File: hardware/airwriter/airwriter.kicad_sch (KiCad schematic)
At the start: 56 parts, among them J1 USB-C 5V in, J2 Mini-DIN-8 to printer, J3 Bring-up USB/UART, J4 Mini-DIN-8 LocalTalk, J6 I2C / Qwiic, SW1 CONFIG/BOOT, SW2 MODE/TEST, U1 ESP32-S3-WROOM-1-N8R2, U2 MAX3490ESA+, U3 MAX3232ESE+, U4 AP7361C-33E, U5 USBLC6-2SC6, U6 SP3485EN-L, U7 PIC12F1840-I/P, U8 SP3485EN-L

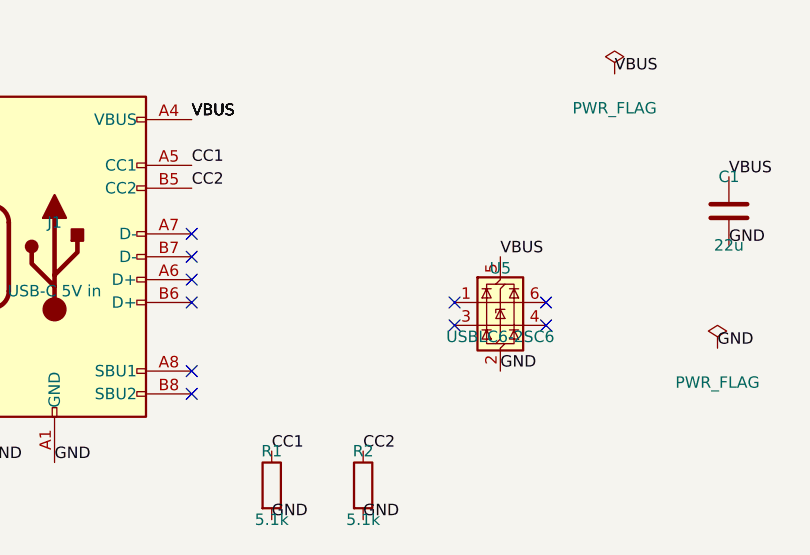
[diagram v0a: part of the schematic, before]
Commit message: Make the USB-C an actual USB port
Spec 2.5 read "USB-C is power only. Flashing and console go over the S3's native USB
peripheral on GPIO19/20 -- expose those on a 4-pin 1.27mm header for bring-up." The
result was a USB connector on the front panel with its data pins tied off, a debug
header nobody can reach without a custom cable, and a two-line USB ESD part sitting
there with four of its six pins no-connected.

D+ and D- now run from J1 through U5 to the S3's native USB peripheral. Both flip
orientations are tied -- A6+B6 and A7+B7 -- which is what a USB 2.0-only device does.
U5's I/O1 is pins 1 and 6 and its I/O2 is pins 3 and 4; each pair is one node inside
the package, so both pins carry the same net and the layout routes through the part.

U5 also moved to sit 2-4mm from J1's data pins instead of 16.7mm, swapping places
with the CC pulldowns. Trace inductance ahead of a clamp is what lets a strike
through, so the ESD part belongs closest to the connector; R1 and R2 only carry a DC
level and can sit further back.

J3 stays as a parallel tap on the same two nets, so there is still a bring-up path if
the connector's data side has a problem on the first spin. J1's silkscreen now reads
USB-C rather than 5V IN, which stopped being true.

Only the S3's native USB is on these pins -- full speed, 12 Mbps -- so the ~60mm run
from J1 to U1 needs no length matching and no impedance control.

SPEC 2.5 amended in place. ERC unchanged at four pre-existing warnings, DRC back to
the single known U1 library mismatch, drill floor 0.300mm, fab regenerated.
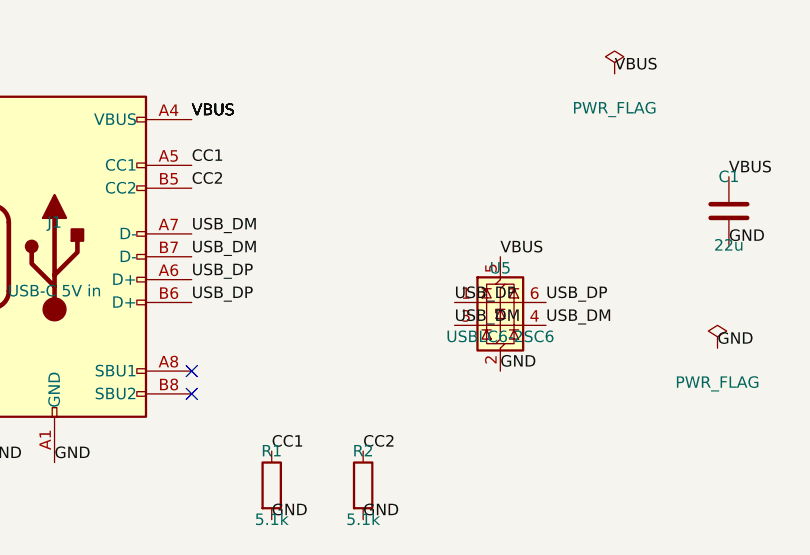
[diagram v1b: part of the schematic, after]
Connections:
- net USB_DM: now also J1.A7 (D-), J1.B7 (D-), U5.3 (I/O2), U5.4 (I/O2)
- net USB_DP: now also J1.A6 (D+), J1.B6 (D+), U5.1 (I/O1), U5.6 (I/O1)
- no-connect marks 39 -> 31
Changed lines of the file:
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@@
   (generator_version "10.0")
   (paper "A3")
-  (no_connect
-    (at 50.8 57.15)
+  (label "USB_DM"
+    (at 50.8 57.15 0)
+    (effects
+      (font
+        (size 1.27 1.27))
+      (justify left bottom))
 )
-  (no_connect
-    (at 50.8 59.69)
+  (label "USB_DM"
+    (at 50.8 59.69 0)
+    (effects
+      (font
+        (size 1.27 1.27))
+      (justify left bottom))
 )
-  (no_connect
-    (at 50.8 62.23)
+  (label "USB_DP"
+    (at 50.8 62.23 0)
+    (effects
+      (font
+        (size 1.27 1.27))
+      (justify left bottom))
 )
-  (no_connect
-    (at 50.8 64.77)
+  (label "USB_DP"
+    (at 50.8 64.77 0)
+    (effects
+      (font
+        (size 1.27 1.27))
+      (justify left bottom))
 )
   (no_connect
@@
     (at 50.8 74.93)
 )
-  (no_connect
-    (at 80.01 64.77)
+  (label "USB_DP"
+    (at 80.01 64.77 0)
+    (effects
+      (font
+        (size 1.27 1.27))
+      (justify left bottom))
+)
+  (label "USB_DM"
+    (at 80.01 67.31 0)
+    (effects
+      (font
+        (size 1.27 1.27))
+      (justify left bottom))
+)
+  (label "USB_DP"
+    (at 90.17 64.77 0)
+    (effects
+      (font
+        (size 1.27 1.27))
+      (justify left bottom))
+)
+  (label "USB_DM"
+    (at 90.17 67.31 0)
+    (effects
+      (font
+        (size 1.27 1.27))
+      (justify left bottom))
 )
   (no_connect
-    (at 80.01 67.31)
-)
-  (no_connect
-    (at 90.17 64.77)
-)
-  (no_connect
-    (at 90.17 67.31)
-)
-  (no_connect

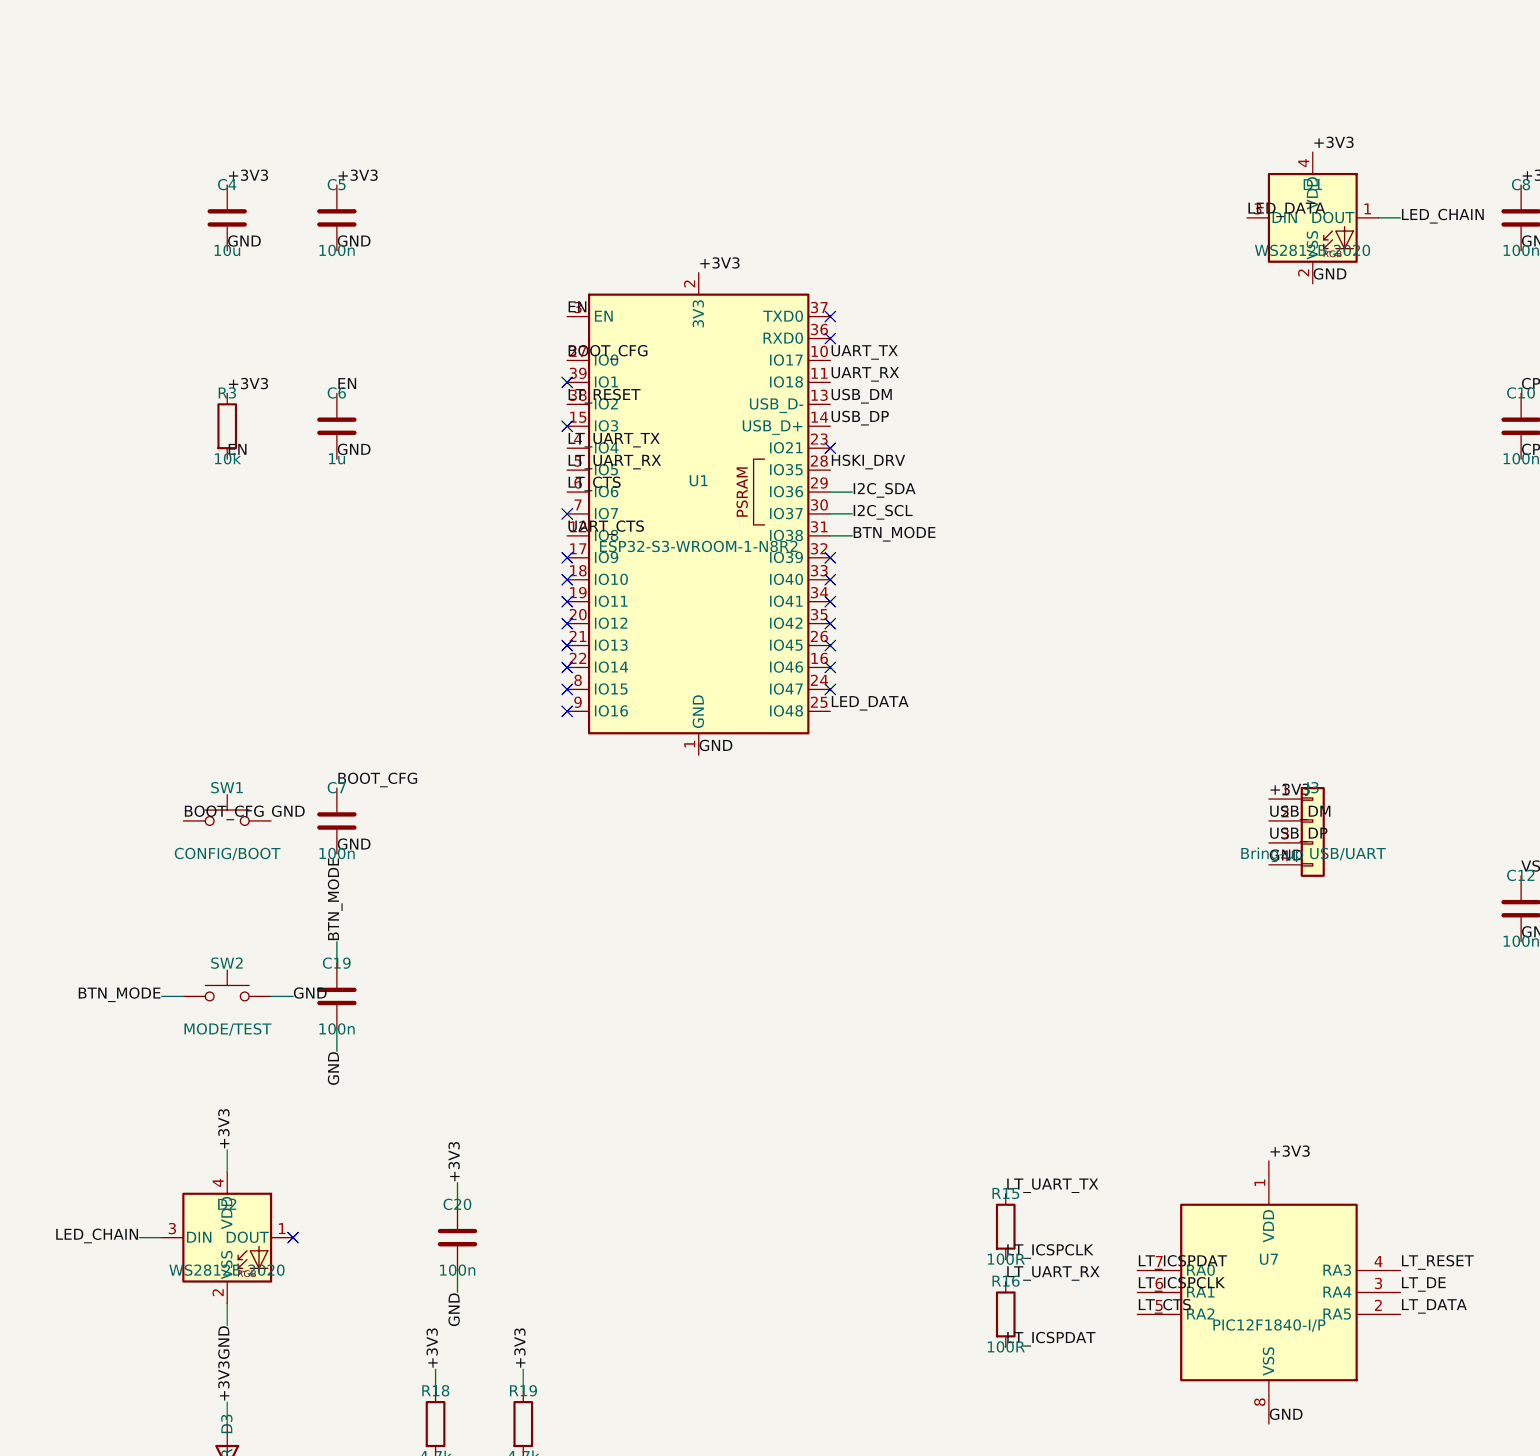
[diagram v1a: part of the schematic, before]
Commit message: Point the indicators at the viewer and make BOOT two pads
Components sit on the face that becomes the underside, so every indicator was firing
away from the person looking at the board. All three are reverse-mount now, emitting
toward the board -- and instead of the hole their footprints expect, they shine into
a bare-FR4 window, which is the logo recipe at small scale.

  D1, D2   WS2812B-2020  ->  SK6812MINI-E   LCSC C5149201, $0.045
  D3       0603 green    ->  LED_1206 ReverseMount
  SW1      B3U-1000P     ->  two bare pads, SolderJumper-2_P1.3mm_Open

The pin numbering changed and the wiring did not. WS2812B-2020 numbers its pins
DOUT-VSS-DIN-VDD; SK6812 numbers them VSS-DIN-VDD-DOUT. But both KiCad symbols put
the same functions at the same coordinates, so swapping lib_id moved every net
correctly and not one label had to move. Checked against the exported netlist.
Firmware is untouched -- SK6812 is the same one-wire protocol at the same 800kbit/s.

BOOT stops being a switch. With the USB-C carrying data, esptool drives the S3 into
download mode over the wire, so the two pads are just insurance you bridge with
tweezers. It also removes the last part that would have wanted a hole in the visible
face. MODE stays a real switch and still faces into the housing; that one is open.

The strip re-spaced -- the SK6812MINI-E is 7.3mm wide against the WS2812B's 3.0 -- and
now runs x 108.9 to 136.3, between mounting hole H3 and the power column.

New trap, documented: D1, D2 and D3 report lib_footprint_mismatch on purpose. Their
library footprints carry a cutout (Edge.Cuts on the SK6812, an NPTH slot on the 1206)
because they are drawn to shine through a hole. Re-importing any of them will punch
the holes back in, same as U1's 0.30mm vias.

DRC is 4 violations and all four are that mismatch. Drill floor 0.300mm, fab
regenerated, ERC unchanged bar the two expected flattened-symbol warnings.
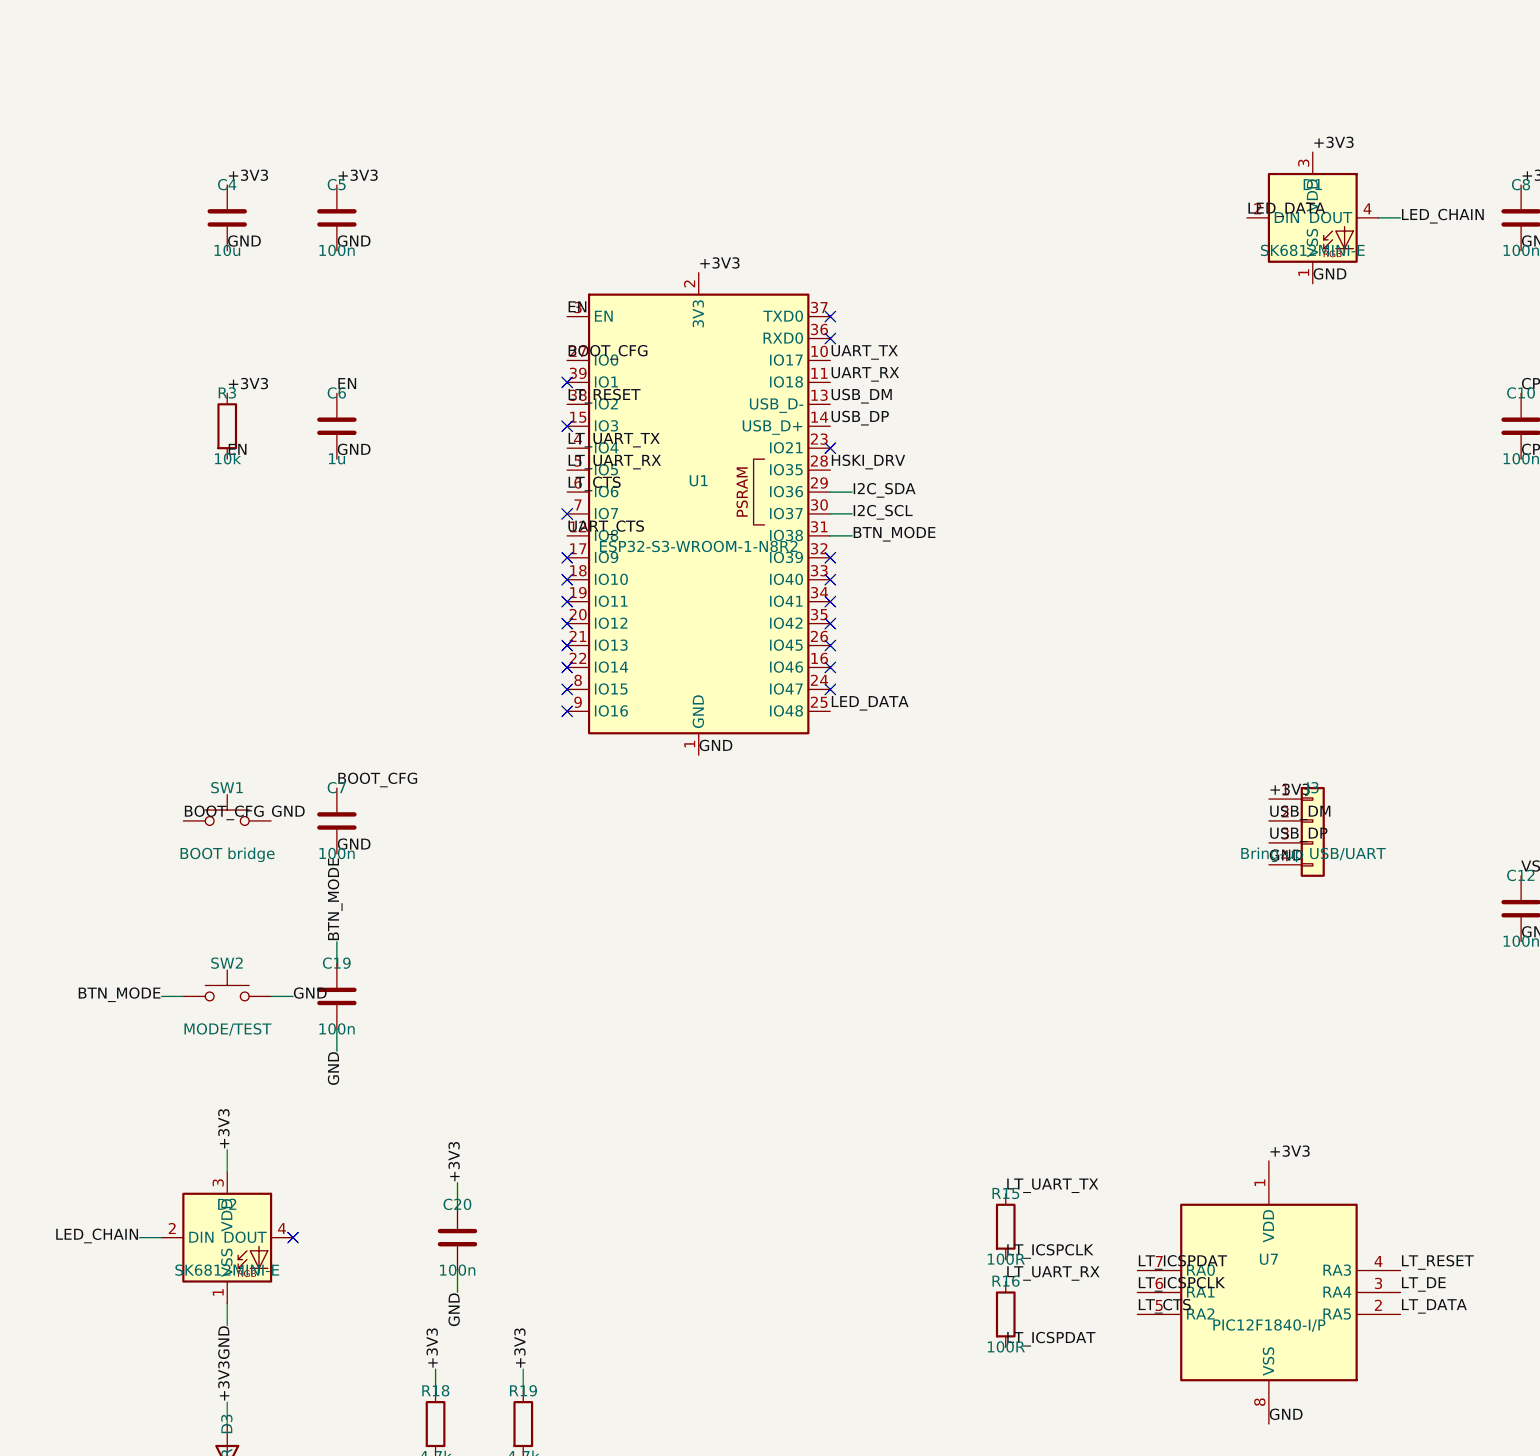
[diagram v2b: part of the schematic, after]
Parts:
- D1, D2: value WS2812B-2020 -> SK6812MINI-E; footprint LED_SMD:LED_WS2812B-2020_PLCC4_2.0x2.0mm -> LED_SMD:LED_SK6812MINI-E_3.2x2.8mm_P1.5mm_ReverseMount; symbol LED:WS2812B-2020 -> LED:SK6812MINI-E; MPN WS2812B-2020 -> SK6812MINI-E; Manufacturer Worldsemi -> OPSCO Optoelectronics
- D3: footprint LED_SMD:LED_0603_1608Metric -> LED_SMD:LED_1206_3216Metric_ReverseMount_Hole1.8x2.4mm
- SW1: value CONFIG/BOOT -> BOOT bridge; footprint Button_Switch_SMD:SW_SPST_B3U-1000P -> Jumper:SolderJumper-2_P1.3mm_Open_Pad1.0x1.5mm; MPN B3U-1000P -> (none); Manufacturer Omron -> none - bare pads on the board
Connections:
- net +3V3: now also D1.3 (VDD), D2.3 (VDD); no longer D1.4 (VDD), D2.4 (VDD)
- net GND: now also D1.1 (VSS), D2.1 (VSS); no longer D1.2 (VSS), D2.2 (VSS)
- net LED_CHAIN: now also D1.4 (DOUT), D2.2 (DIN); no longer D1.1 (DOUT), D2.3 (DIN)
- net LED_DATA: now also D1.2 (DIN); no longer D1.3 (DIN)
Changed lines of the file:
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@@
         (font
           (size 1.27 1.27))))
-    (property "Value" "CONFIG/BOOT"
+    (property "Value" "BOOT bridge"
       (at 149.86 179.07 0)
       (effects
         (font
           (size 1.27 1.27))))
-    (property "Footprint" "Button_Switch_SMD:SW_SPST_B3U-1000P"
+    (property "Footprint" "Jumper:SolderJumper-2_P1.3mm_Open_Pad1.0x1.5mm"
       (at 149.86 175.26 0)
       (hide yes)
@@
         (font
           (size 1.27 1.27))))
-    (property "MPN" "B3U-1000P"
+    (property "MPN" ""
       (at 149.86 171.45 0)
       (hide yes)
@@
         (font
           (size 1.27 1.27))))
-    (property "Manufacturer" "Omron"
+    (property "Manufacturer" "none - bare pads on the board"
       (at 149.86 171.45 0)
       (hide yes)
@@
         (font
           (size 1.27 1.27))))
-    (property "Description" "Tactile switch SPST-NO, SMD, ultra-small"
+    (property "Description" "Two exposed pads, normally open. Bridge with tweezers to force download mode; the USB-C port normally does this without them"
       (at 149.86 171.45 0)
       (hide yes)
@@
           (unit 1)))))
   (symbol
-    (lib_id "LED:WS2812B-2020")
+    (lib_id "LED:SK6812MINI-E")
     (at 275.59 105.41 0)
     (unit 1)
@@
         (font
           (size 1.27 1.27))))
-    (property "Value" "WS2812B-2020"
+    (property "Value" "SK6812MINI-E"
       (at 275.59 109.22 0)
       (effects
         (font
           (size 1.27 1.27))))
-    (property "Footprint" "LED_SMD:LED_WS2812B-2020_PLCC4_2.0x2.0mm"
+    (property "Footprint" "LED_SMD:LED_SK6812MINI-E_3.2x2.8mm_P1.5mm_ReverseMount"
       (at 275.59 105.41 0)
       (hide yes)
@@
         (font
           (size 1.27 1.27))))
-    (property "MPN" "WS2812B-2020"
+    (property "MPN" "SK6812MINI-E"
       (at 275.59 101.6 0)
       (hide yes)
@@
         (font
           (size 1.27 1.27))))
-    (property "Manufacturer" "Worldsemi"
+    (property "Manufacturer" "OPSCO Optoelectronics"
       (at 275.59 101.6 0)
       (hide yes)
@@
         (font
           (size 1.27 1.27))))
-    (property "Description" "RGB LED, integrated controller, 2.0 x 2.0mm"
+    (property "Description" "Addressable RGB LED, reverse mount. Fires up through the board into a bare-FR4 window, no hole"
       (at 275.59 101.6 0)
       (hide yes)
@@
           (unit 1)))))
   (symbol
-    (lib_id "LED:WS2812B-2020")
+    (lib_id "LED:SK6812MINI-E")
     (at 149.86 223.52 0)
     (unit 1)
@@
         (font
           (size 1.27 1.27))))
-    (property "Value" "WS2812B-2020"
+    (property "Value" "SK6812MINI-E"
       (at 149.86 227.33 0)
       (effects
         (font
           (size 1.27 1.27))))
-    (property "Footprint" "LED_SMD:LED_WS2812B-2020_PLCC4_2.0x2.0mm"
+    (property "Footprint" "LED_SMD:LED_SK6812MINI-E_3.2x2.8mm_P1.5mm_ReverseMount"
       (at 149.86 223.52 0)
       (hide yes)
@@
         (font
           (size 1.27 1.27))))
-    (property "MPN" "WS2812B-2020"
+    (property "MPN" "SK6812MINI-E"
       (at 149.86 223.52 0)
       (hide yes)
@@
         (font
           (size 1.27 1.27))))
-    (property "Manufacturer" "Worldsemi"
+    (property "Manufacturer" "OPSCO Optoelectronics"
       (at 149.86 223.52 0)
       (hide yes)
@@
         (font
           (size 1.27 1.27))))
-    (property "Description" "Addressable RGB LED, 2020, chained from D1's DOUT"
+    (property "Description" "Addressable RGB LED, reverse mount. Fires up through the board into a bare-FR4 window, no hole"
       (at 149.86 223.52 0)
       (hide yes)
@@
         (font
           (size 1.27 1.27))))
-    (property "Footprint" "LED_SMD:LED_0603_1608Metric"
+    (property "Footprint" "LED_SMD:LED_1206_3216Metric_ReverseMount_Hole1.8x2.4mm"
       (at 149.86 248.92 0)
       (hide yes)
@@
         (font
           (size 1.27 1.27))))
-    (property "Description" "Green LED, 0603, power rail indicator"
+    (property "Description" "Green power LED, reverse mount. Fires up through the board into a bare-FR4 window"
       (at 149.86 248.92 0)
       (hide yes)
